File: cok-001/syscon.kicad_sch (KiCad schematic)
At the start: 140 parts, among them J4001 FAN, J4003 Conn_01x02_Pin, J4009 Conn_01x30_Socket, J4010 BUTTONS, Q4008 DTC144E, Q4011 DTC143ZUA, Q4012 UMH2NTN, Q4013 UMH2NTN, Q4014 DTC143ZUA, Q4015 DTC143ZUA, U4003 74LVC2G34, U4004 74LVC2G34, U4005 74LVC2G34, U4006 74LVC1G34, Y4001 16.9344MHz, Y4002 32.768kHz

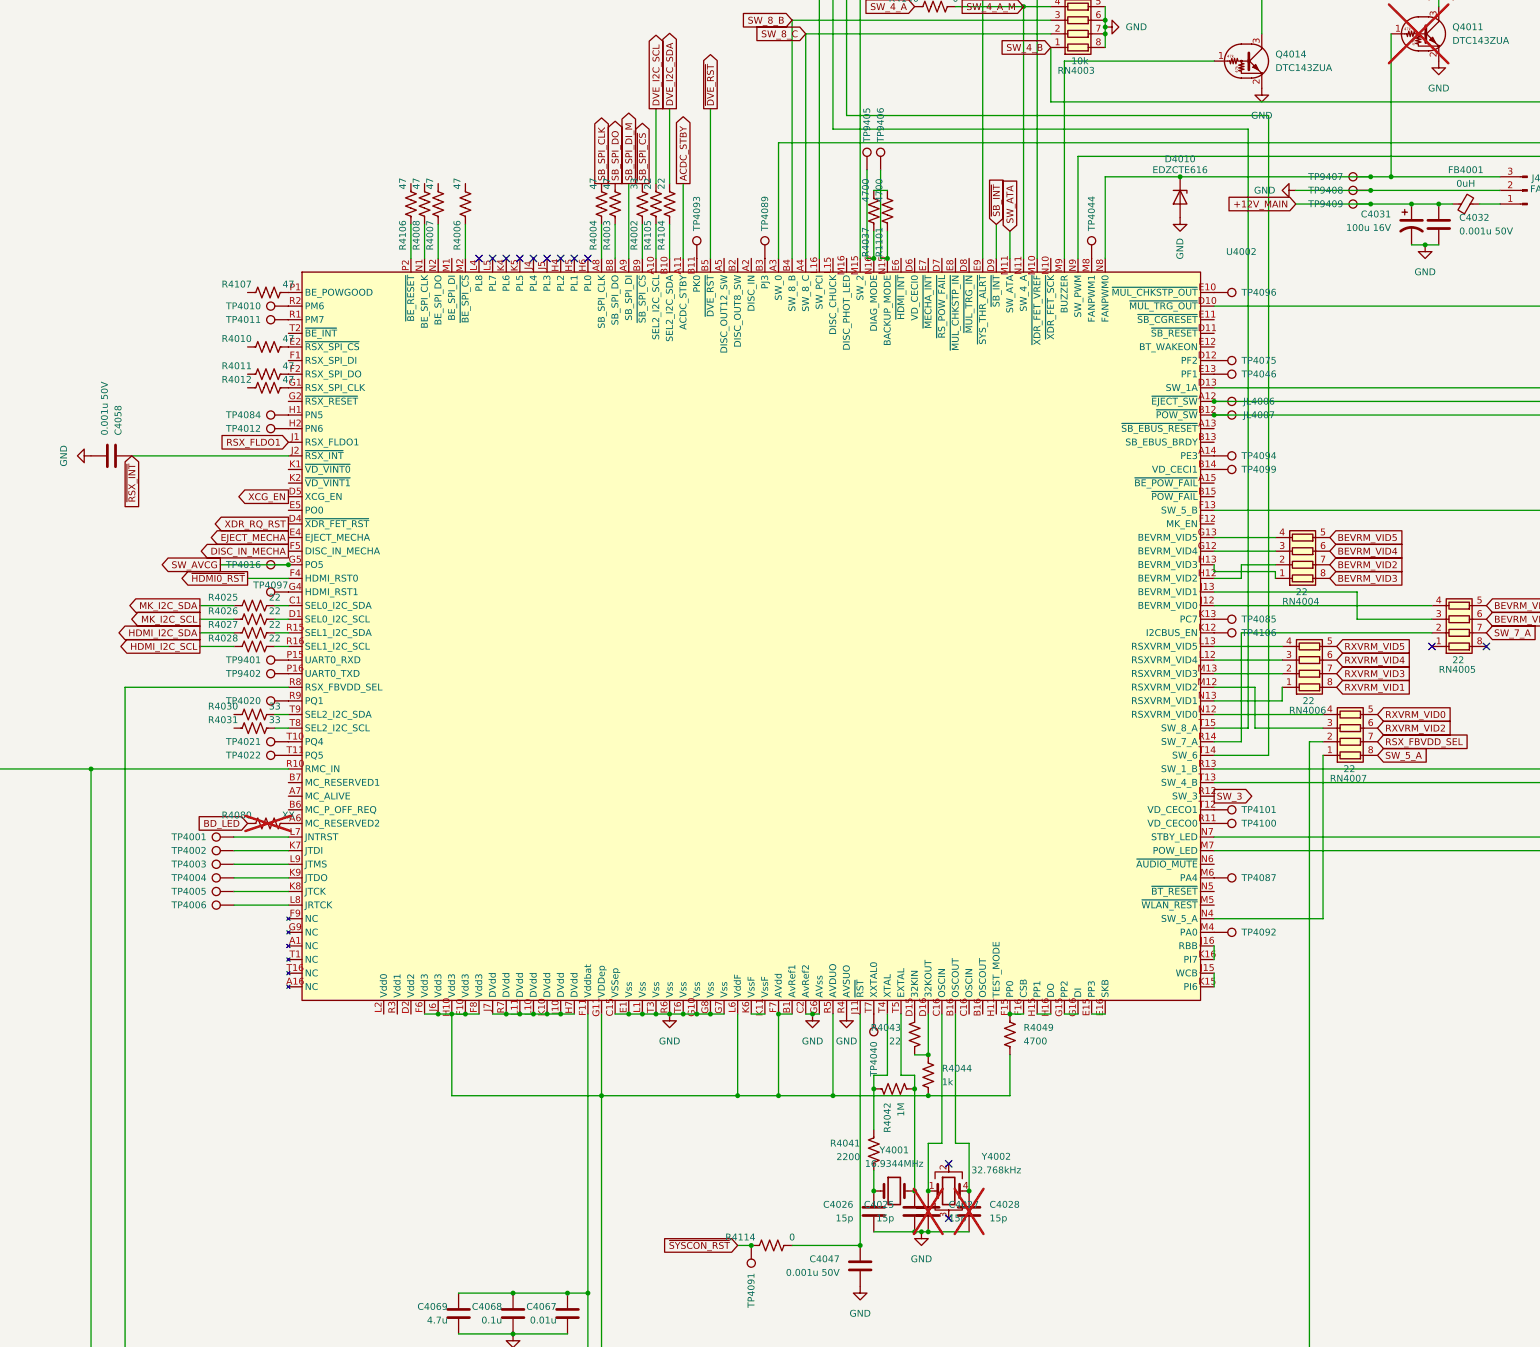
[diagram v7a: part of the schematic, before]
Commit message: wireless reset
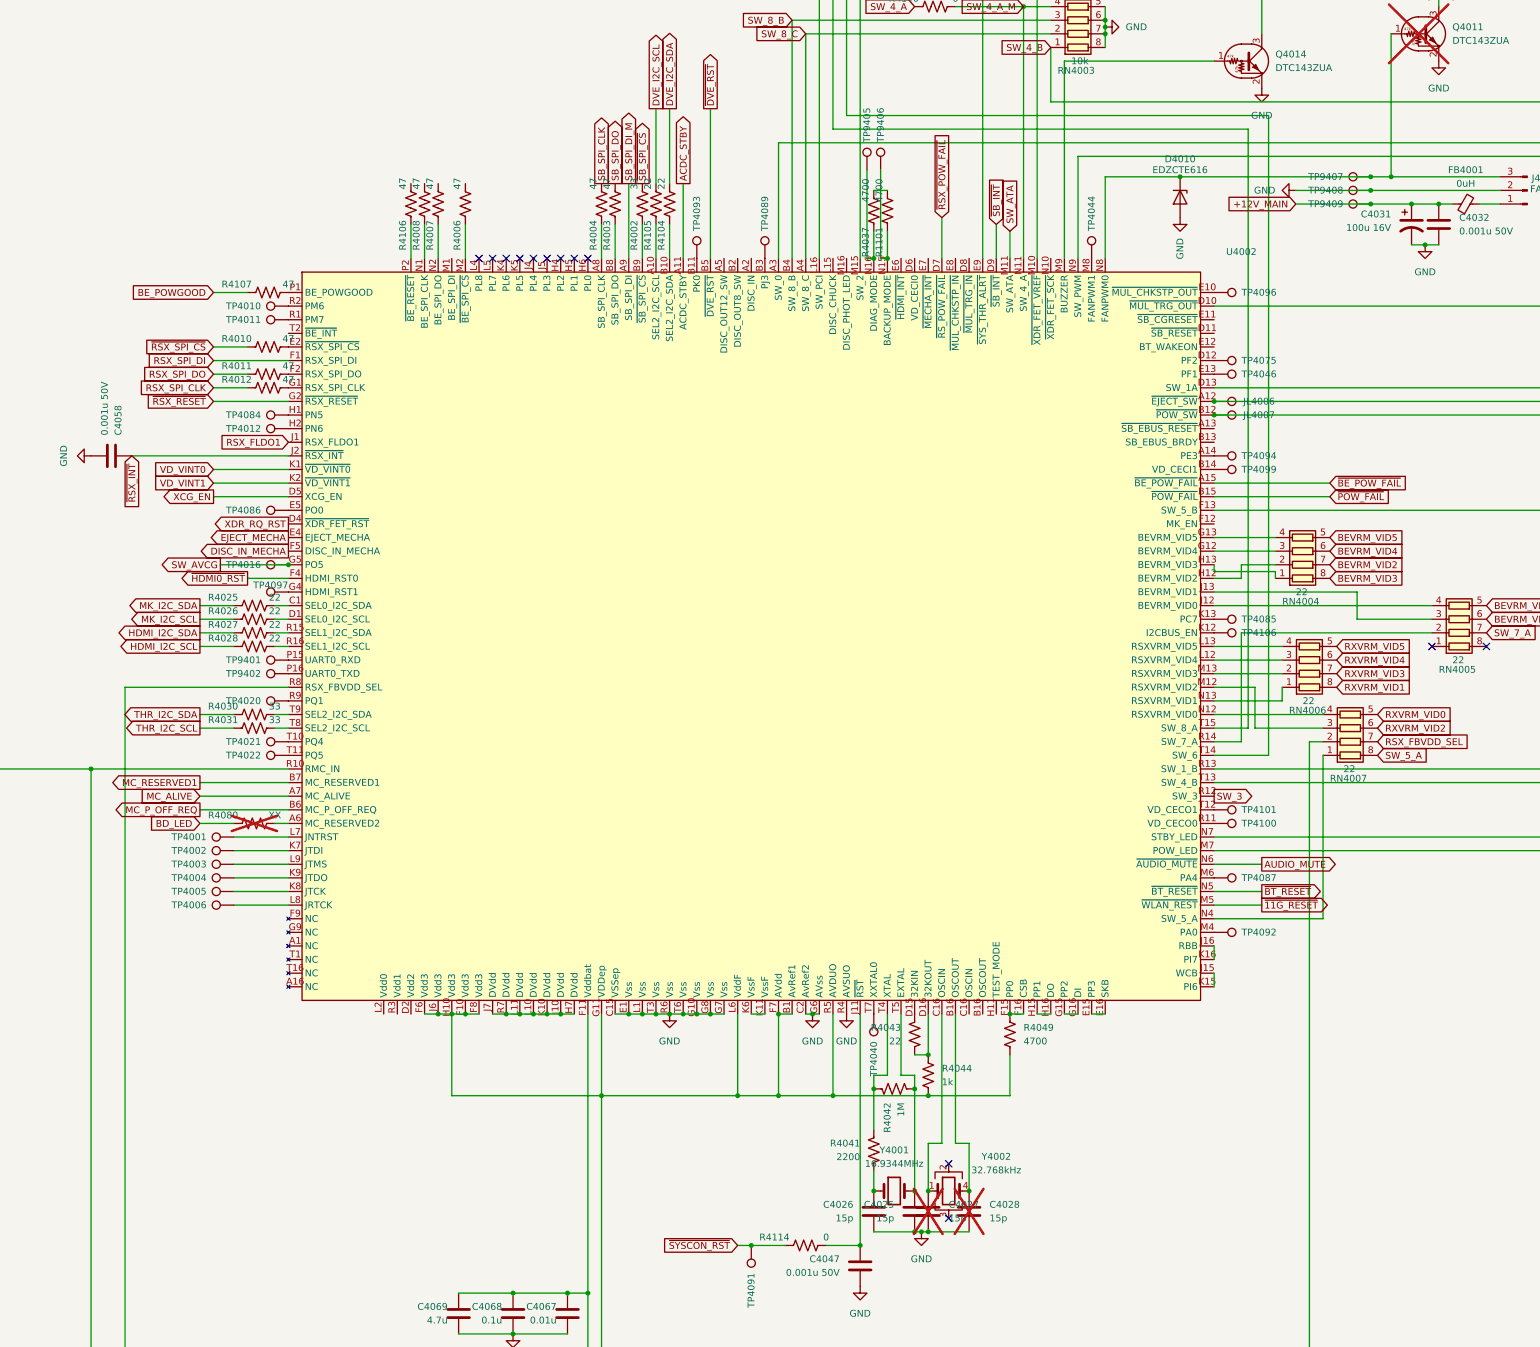
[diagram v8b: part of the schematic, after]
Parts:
- added TP4086: TestPoint, TestPoint:TestPoint_Pad_1.0x1.0mm, symbol Connector:TestPoint
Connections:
- net MC_ALIVE: now also U4002.A7 (MC_ALIVE)
- net THR_I2C_SCL: now reaches R4031.1
- net RSX_SPI_CLK: now reaches R4012.1
- net ~{RSX_SPI_CS}: now reaches R4010.1
- net THR_I2C_SDA: now reaches R4030.1
- net ~{BE_POW_FAIL}: now reaches U4002.A15 (~{BE_POW_FAIL})
- net ~{POW_FAIL}: now reaches U4002.B15 (~{POW_FAIL})
- net MC_P_OFF_REQ: now reaches U4002.B6 (MC_P_OFF_REQ)
- net MC_RESERVED1: now reaches U4002.B7 (MC_RESERVED1)
- net at U4002.C16 (OSCIN): now also C4027.1, Y4002.1
- net ~{RSX_POW_FAIL}: now reaches U4002.D7 (~{RS_POW_FAIL})
- net at U4002.E5 (PO0): now also TP4086.1
- net RSX_SPI_DI: now reaches U4002.F1 (RSX_SPI_DI)
- net ~{RSX_RESET}: now reaches U4002.G2 (~{RSX_RESET})
- net VD_VINT0: now reaches U4002.K1 (~{VD_VINT0})
- net VD_VINT1: now reaches U4002.K2 (~{VD_VINT1})
- net ~{11G_RESET}: now reaches U4002.M5 (~{WLAN_REST})
- net ~{BT_RESET}: now reaches U4002.N5 (~{BT_RESET})
- net AUDIO_MUTE: now reaches U4002.N6 (~{AUDIO_MUTE})
- net RSX_SPI_DO: now reaches R4011.1
- net BE_POWGOOD: now reaches R4107.1
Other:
- moved on the sheet: R4080, R4114
